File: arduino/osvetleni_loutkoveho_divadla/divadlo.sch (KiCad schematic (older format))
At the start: 11 parts, among them IC1 ATMEGA32-P

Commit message: meziverze
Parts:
- removed LED1, LED2, LED3, LED4: CONN_4, symbol CONN_4
- added 1, 2, 3, 4: 5MMRGBLED, SIL-4, symbol 5MMRGBLED
- added P1: CONN_8, SIL-8, symbol CONN_8
- added R1, R2, R3, R4: R, symbol R
- added RV1, RV2, RV3: POT, 3PIN_6mm, symbol POT
- IC1: footprint DIL40 -> DIP-24__300
- POT-B1: renamed from POT-B; footprint (none) -> POT_CMS
- POT-G1: renamed from POT-G; footprint (none) -> POT_CMS
- POT-R1: renamed from POT-R; footprint (none) -> RV2X4
- Q1, Q2, Q3: renamed from Q?; footprint TO92-EBC -> TO220
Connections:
- net labels added: HT
- wire segments 53 -> 115
- no-connect marks 0 -> 24

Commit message: nahrada chybneho AVR, ruzne zmeny pouzder, atd.
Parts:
- removed IC1: ATMEGA32-P, DIP-24__300, symbol ATMEGA32-P
- removed R2, R4: R, symbol R
- added IC1: ATMEGA48/88/168-PU, atmega8-DIL28-3, symbol ATMEGA48/88/168-PU
- added R1: 4k7, symbol R
- P1: value CONN_8 -> ICSP+SERIAL_ISP
- POT-B1, POT-G1, POT-R1: value POT -> 10K
- POT1: renamed from RV1; value POT -> SYTOST
- POT2: renamed from RV2; value POT -> JAS
- POT3: renamed from RV3; value POT -> BARVA
- Q1, Q2, Q3: value BC237 -> BD139-16
- R2: renamed from R1; value R -> 1M
- R3: value R -> 1M
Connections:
- net labels added: VCC
- net labels removed: +BATT, HT
- wire segments 115 -> 116
- no-connect marks 24 -> 8
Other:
- moved on the sheet: R2

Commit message: opravena verze
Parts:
- removed P1: ICSP+SERIAL_ISP, SIL-8, symbol CONN_8
- added C1: 100n, symbol C
- added P1: mereni_LED, symbol CONN_3X2
- added P2: ISP_via_arduino, symbol CONN_5
- added P3: napajeni, symbol CONN_2
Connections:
- net at 1.4 (RED), 2.4 (RED), 3.4 (RED)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: now also P1.2; no longer Q1.E
- net at 1.1 (BLUE), 2.1 (BLUE), 3.1 (BLUE)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: now also P1.6; no longer Q3.E
- net at 1.2 (GREEN), 2.2 (GREEN), 3.2 (GREEN)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: now also P1.4; no longer Q2.E
- net at IC1.2 (PD0(RXD/PCINT16)): now also P2.3
- net at IC1.3 (PD1(TXD/PCINT17)): now also P2.2
- net at IC1.1 (PC6(/RESET/PCINT14)), R1.1: now also C1.2
- net GND: no longer names the net of 1.3 (GND), 2.3 (GND), 3.3 (GND), 4.3 (GND), IC1.22 (AGND), IC1.8 (GND@1), POT1.3, POT2.3, POT3.3
- net GND: now also P2.4, P3.1 (P1)
- net VCC: no longer names the net of IC1.20 (AVCC), IC1.7 (VCC@1), POT1.1, POT2.1, POT3.1, Q1.C, Q2.C, Q3.C, R1.2
- net VCC: now also P2.1, P3.2 (PM)
- new net: P1.1, Q1.E
- new net: P1.3, Q2.E
- new net: P1.5, Q3.E
- new net: C1.1, P2.5
- no-connect marks 8 -> 11

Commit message: plosnak
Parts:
- removed P1: mereni_LED, symbol CONN_3X2
- removed R2, R3: 1M, symbol R
- added P4: pwr_sel, symbol CONN_3
- added U1: LM7805, symbol LM7805
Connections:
- net at POT-R1.1, POT-R1.2: now also Q1.B; no longer IC1.5 (PD3(INT1/OC2B/PCINT19))
- net at POT-R1.3: now also IC1.12 (PD6(AIN0/OC0A/PCINT22)); no longer Q1.B
- net at POT-G1.1, POT-G1.2: now also Q2.B; no longer IC1.11 (PD5(T1/OC0B/PCINT21))
- net at POT-G1.3: now also IC1.11 (PD5(T1/OC0B/PCINT21)); no longer Q2.B
- net at POT-B1.1, POT-B1.2: now also Q3.B; no longer IC1.12 (PD6(AIN0/OC0A/PCINT22))
- net at POT-B1.3: now also IC1.5 (PD3(INT1/OC2B/PCINT19)); no longer Q3.B
- net at IC1.20 (AVCC), IC1.7 (VCC@1), P2.1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: now also P4.2 (PM); no longer P3.2 (PM)
- net at Q1.E: now also 1.4 (RED), 2.4 (RED), 3.4 (RED), 4.4 (RED)
- net at 1.1 (BLUE), 2.1 (BLUE), 3.1 (BLUE)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: now also Q3.E
- net at 1.2 (GREEN), 2.2 (GREEN), 3.2 (GREEN)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: now also Q2.E
- net at 1.3 (GND), 2.3 (GND), 3.3 (GND)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: now also U1.GND
- net at POT2.2: now also IC1.25 (PC2(ADC2/PCINT10)); no longer IC1.24 (PC1(ADC1/PCINT9))
- net at POT1.2: now also IC1.24 (PC1(ADC1/PCINT9)); no longer IC1.25 (PC2(ADC2/PCINT10))
- new net: P3.2 (PM), P4.1 (P1), U1.VI
- new net: P4.3 (P3), U1.VO
- no-connect marks 11 -> 15
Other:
- moved on the sheet: POT-B1, POT-G1, POT-R1
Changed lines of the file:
@@
-EESchema Schematic File Version 2  date 18.7.2010 16:18:10
+EESchema Schematic File Version 2  date 27.7.2010 20:41:45
 LIBS:power
 LIBS:device
@@
 Sheet 1 1
 Title ""
-Date "18 jul 2010"
+Date "27 jul 2010"
 Rev ""
 Comp ""
@@
 $EndDescr
 Wire Wire Line
+	3650 3250 3825 3250
+Wire Wire Line
+	3825 3250 3825 3075
+Wire Wire Line
+	3650 4350 3725 4350
+Wire Wire Line
+	3725 4350 3725 6525
+Wire Wire Line
+	6375 5425 6375 4350
+Wire Wire Line
+	6625 6125 6875 6125
+Wire Wire Line
+	6875 6125 6875 5975
+Wire Wire Line
+	8400 4300 9400 4300
+Connection ~ 4800 2500
+Wire Wire Line
+	4800 2350 4800 2750
+Wire Wire Line
+	4800 2750 6450 2750
+Wire Wire Line
+	6450 2750 6450 2650
+Wire Wire Line
+	5700 2350 5900 2350
+Wire Wire Line
+	5900 2350 5900 2100
+Wire Wire Line
+	5900 2100 6850 2100
+Wire Wire Line
+	6850 2100 6850 2350
+Wire Wire Line
+	5000 2350 5500 2350
+Wire Wire Line
 	4575 7125 10325 7125
 Wire Wire Line
@@
 	9475 3800 9475 4400
 Wire Wire Line
-	9475 4400 9350 4400
-Wire Wire Line
 	8400 3150 8400 4025
-Wire Wire Line
-	8550 4300 8400 4300
 Wire Wire Line
 	8400 4300 8400 6175
@@
 	9975 6500 10325 6500
 Connection ~ 3850 2650
-Wire Wire Line
-	750  2650 5000 2650
 Connection ~ 4150 2500
-Wire Wire Line
-	4800 2350 4800 2500
 Wire Wire Line
 	4800 2500 650  2500
@@
 	4050 2700 4050 2400
 Wire Wire Line
-	750  2650 750  4550
+	750  4550 750  2650
 Wire Wire Line
 	3850 2400 3850 2650
 Wire Wire Line
-	3650 4250 3875 4250
-Wire Wire Line
-	3875 4250 3875 4650
-Wire Wire Line
-	3875 4650 4275 4650
-Wire Wire Line
-	3650 4450 3825 4450
-Wire Wire Line
-	3825 4450 3825 4850
-Wire Wire Line
-	3825 4850 4275 4850
-Wire Wire Line
-	3650 4650 3725 4650
-Wire Wire Line
-	3725 4650 3725 6525
-Wire Wire Line
 	3725 6525 6375 6525
 Wire Wire Line
@@
 	3775 5975 6375 5975
 Wire Wire Line
-	3650 4350 6375 4350
-Wire Wire Line
 	3650 4150 3950 4150
-Wire Wire Line
-	3650 3350 3825 3350
-Wire Wire Line
-	3825 3350 3825 3075
 Wire Wire Line
 	3825 3075 4325 3075
@@
 Wire Wire Line
 	750  4550 1250 4550
-Wire Wire Line
-	5075 4850 4775 4850
 Connection ~ 4575 3850
 Connection ~ 4575 3550
@@
 Connection ~ 4575 6850
 Wire Wire Line
-	6375 6525 6375 6375
-Wire Wire Line
-	6375 6375 6625 6375
-Wire Wire Line
-	6625 5275 6375 5275
-Wire Wire Line
 	9475 4600 9475 6850
 Wire Wire Line
@@
 Wire Wire Line
 	8400 6175 7175 6175
-Connection ~ 6375 5975
 Connection ~ 4075 3850
 Wire Wire Line
 	8975 6300 8975 6850
 Connection ~ 8975 6850
-Wire Wire Line
-	4775 4850 4775 4950
-Wire Wire Line
-	4775 4650 4775 4750
-Wire Wire Line
-	4775 4650 5075 4650
 Connection ~ 750  4550
 Wire Wire Line
@@
 	4325 3400 3775 3400
 Wire Wire Line
-	3775 3400 3775 3250
-Wire Wire Line
-	3775 3250 3650 3250
-Wire Wire Line
 	3900 4050 3650 4050
-Wire Wire Line
-	6375 4350 6375 5425
-Connection ~ 6375 5275
-Wire Wire Line
-	6375 5975 6375 5825
-Wire Wire Line
-	6375 5825 6625 5825
-Wire Wire Line
-	4775 4950 3650 4950
-Wire Wire Line
-	4775 4750 3650 4750
 Wire Wire Line
 	1250 4250 750  4250
@@
 	4375 2400 4250 2400
 Wire Wire Line
-	5000 2650 5000 2350
-Wire Wire Line
 	7850 5625 7850 4200
 Wire Wire Line
-	7850 4200 8550 4200
-Wire Wire Line
 	8500 3950 8500 3450
 Wire Wire Line
-	9350 4300 9400 4300
-Wire Wire Line
 	9400 4300 9400 4025
 Wire Wire Line
@@
 	8350 6725 8350 4400
 Wire Wire Line
-	8350 4400 8550 4400
-Wire Wire Line
 	8350 3000 8350 3800
 Wire Wire Line
 	7175 2850 750  2850
-$Comp
-L CONN_3X2 P1
-U 1 1 4C430BB9
-P 8950 4350
-F 0 "P1" H 8950 4600 50  0000 C CNN
-F 1 "mereni_LED" V 8950 4400 40  0000 C CNN
-	1    8950 4350
+Wire Wire Line
+	750  2650 5600 2650
+Wire Wire Line
+	5600 2650 5600 2350
+Wire Wire Line
+	6050 2350 6050 2500
+Wire Wire Line
+	6050 2500 5250 2500
+Wire Wire Line
+	5250 2500 5250 2350
+Connection ~ 5250 2350
+Wire Wire Line
+	7850 4200 9350 4200
+Wire Wire Line
+	8350 4400 9475 4400
+Wire Wire Line
+	6625 5575 6875 5575
+Wire Wire Line
+	6875 5575 6875 5425
+Wire Wire Line
+	6875 6525 6875 6675
+Wire Wire Line
+	6875 6675 6625 6675
+Wire Wire Line
+	6375 4350 4025 4350
+Wire Wire Line
+	4025 4350 4025 4650
+Wire Wire Line
+	4025 4650 3650 4650
+Wire Wire Line
+	3775 3400 3775 3350
+Wire Wire Line
+	3775 3350 3650 3350
+NoConn ~ 3650 4950
+NoConn ~ 3650 4750
+NoConn ~ 3650 4450
+NoConn ~ 3650 4250
+$Comp
+L CONN_3 P4
+U 1 1 4C4CA758
+P 5600 2000
+F 0 "P4" V 5550 2000 50  0000 C CNN
+F 1 "pwr_sel" V 5650 2000 40  0000 C CNN
+	1    5600 2000
+	0    -1   -1   0
+$EndComp
+$Comp
+L LM7805 U1
+U 1 1 4C4CA734
+P 6450 2400
+F 0 "U1" H 6600 2204 60  0000 C CNN
+F 1 "LM7805" H 6450 2600 60  0000 C CNN
+	1    6450 2400
 	1    0    0    -1
 $EndComp
@@
 $EndComp
 $Comp
-L R R3
-U 1 1 4C3C22A7
-P 4525 4650
-F 0 "R3" V 4605 4650 50  0000 C CNN
-F 1 "1M" V 4525 4650 50  0000 C CNN
-	1    4525 4650
-	0    1    1    0
-$EndComp
-$Comp
 L BC237 Q3
 U 1 1 4C3C2263
@@
 F 1 "4k7" V 1000 3150 50  0000 C CNN
 	1    1000 3150
-	0    1    1    0
-$EndComp
-$Comp
-L R R2
-U 1 1 4C3AE3B9
-P 4525 4850
-F 0 "R2" V 4605 4850 50  0000 C CNN
-F 1 "1M" V 4525 4850 50  0000 C CNN
-	1    4525 4850
 	0    1    1    0
 $EndComp
@@
 F 2 "POT_CMS" H 6625 6525 60  0001 C CNN
 	1    6625 6525
-	1    0    0    -1
+	-1   0    0    1
 $EndComp
 $Comp
@@
 F 2 "POT_CMS" H 6625 5975 60  0001 C CNN
 	1    6625 5975
-	1    0    0    -1
+	-1   0    0    1
 $EndComp
 $Comp
@@
 F 2 "RV2X4" H 6625 5425 60  0001 C CNN
 	1    6625 5425
-	1    0    0    -1
+	-1   0    0    1
 $EndComp
 $EndSCHEMATC

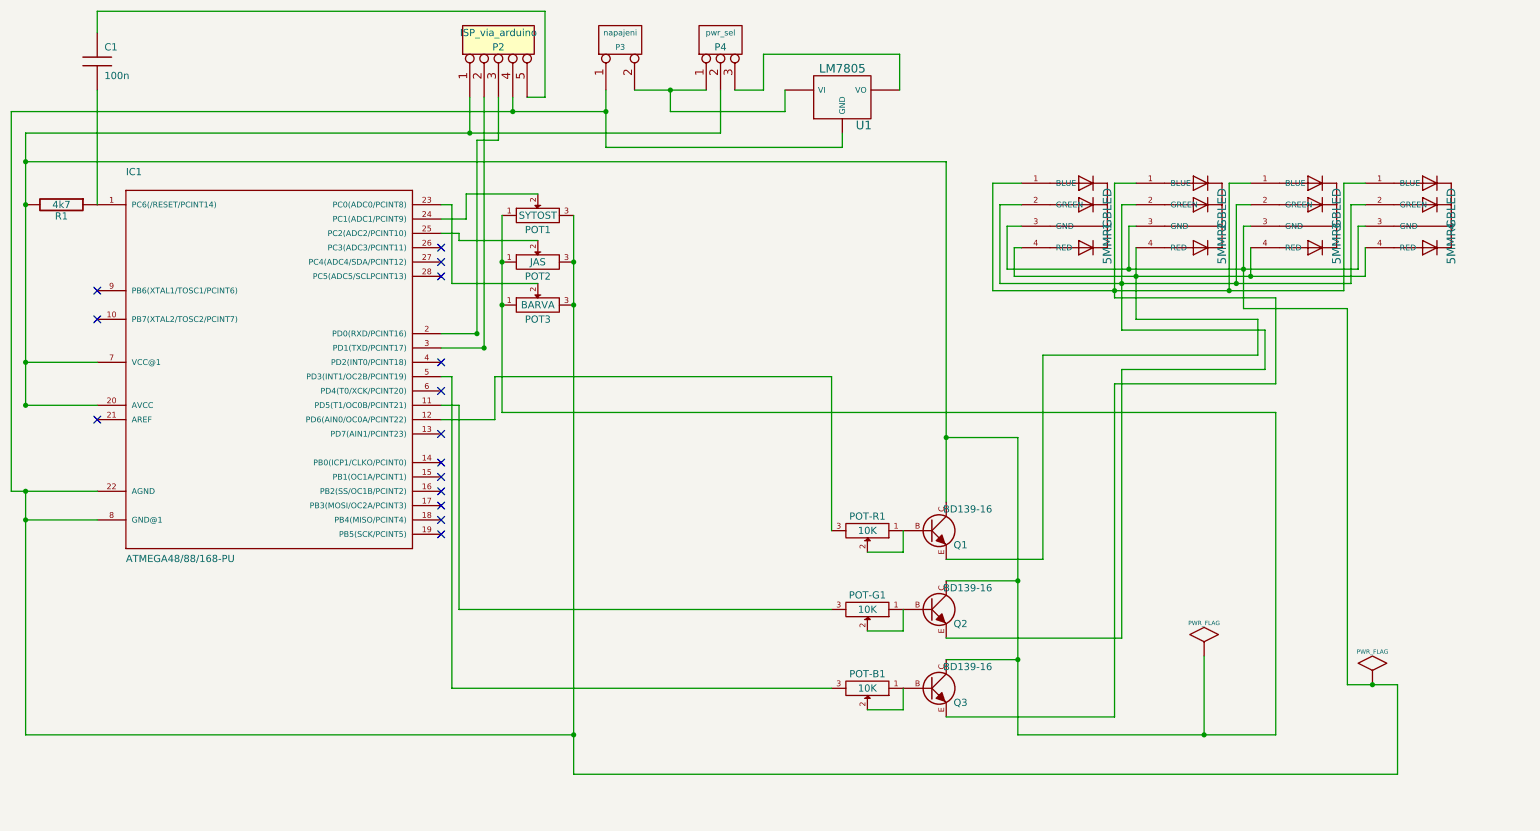
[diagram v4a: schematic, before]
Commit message: nahrada historicke LM7805 za lepsi LF50CV (LDO) + doplneni nutneho kondenzatoru
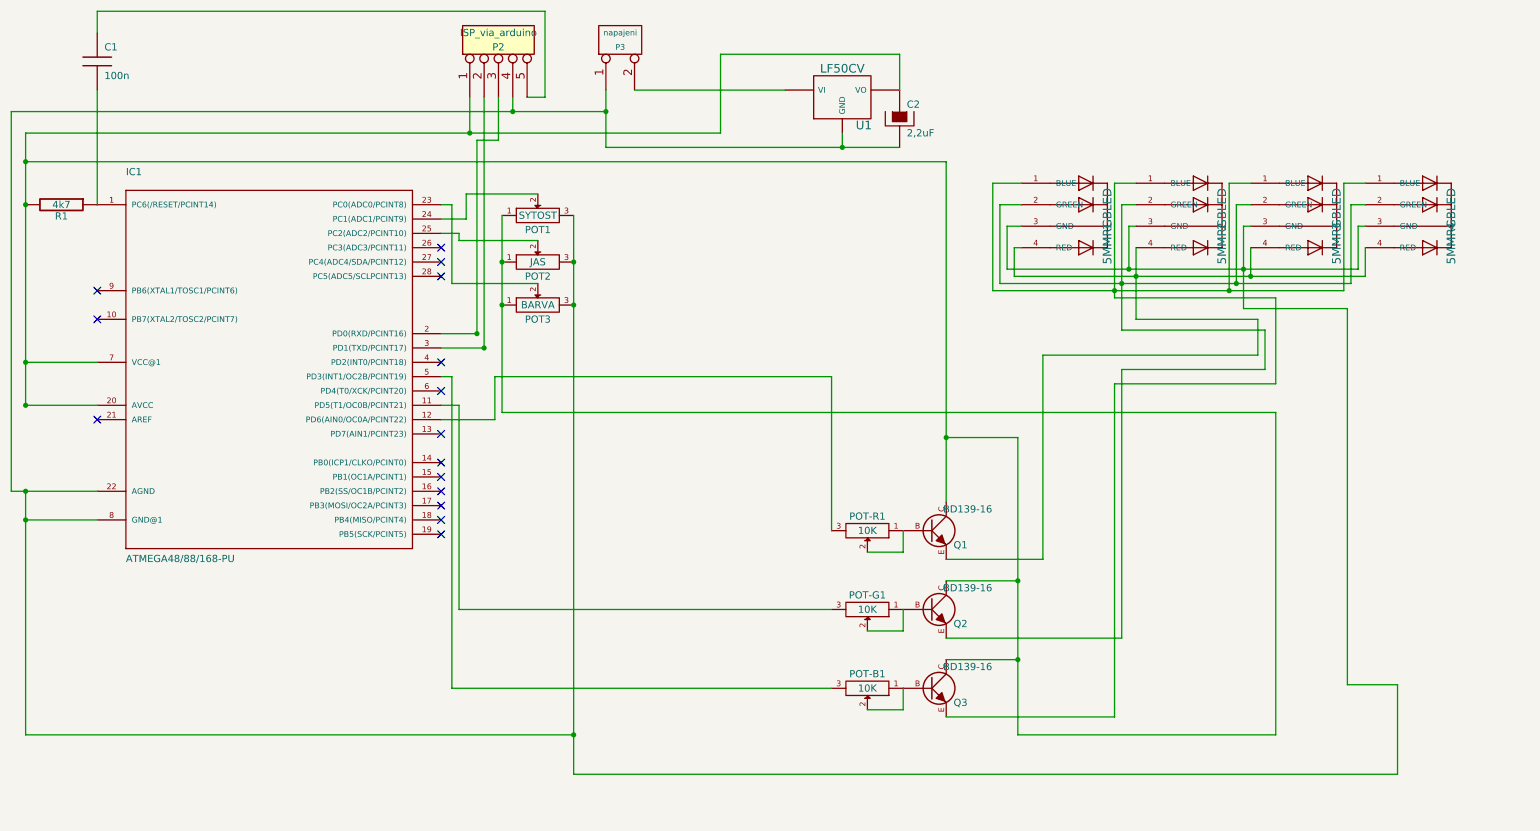
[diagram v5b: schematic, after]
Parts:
- removed P4: pwr_sel, symbol CONN_3
- added C2: 2,2uF, symbol CAPAPOL
- U1: value LM7805 -> LF50CV
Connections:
- net at IC1.20 (AVCC), IC1.7 (VCC@1), P2.1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: now also U1.VO, C2.1
- net at 1.3 (GND), 2.3 (GND), 3.3 (GND)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: now also C2.2
